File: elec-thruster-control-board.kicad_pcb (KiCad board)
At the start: 2 copper layers, 44 parts, among them J11 Conn_01x02_Socket, J12 Conn_01x02_Socket, J13 Conn_02x05_Counter_Clockwise, J15 Conn_01x02_Socket, J16 Conn_01x02_Socket, J18 Conn_01x02_Socket, J19 Conn_01x02_Socket, J2 Conn_01x02_Socket, J20 Conn_01x02_Socket, J21 Conn_01x02_Socket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

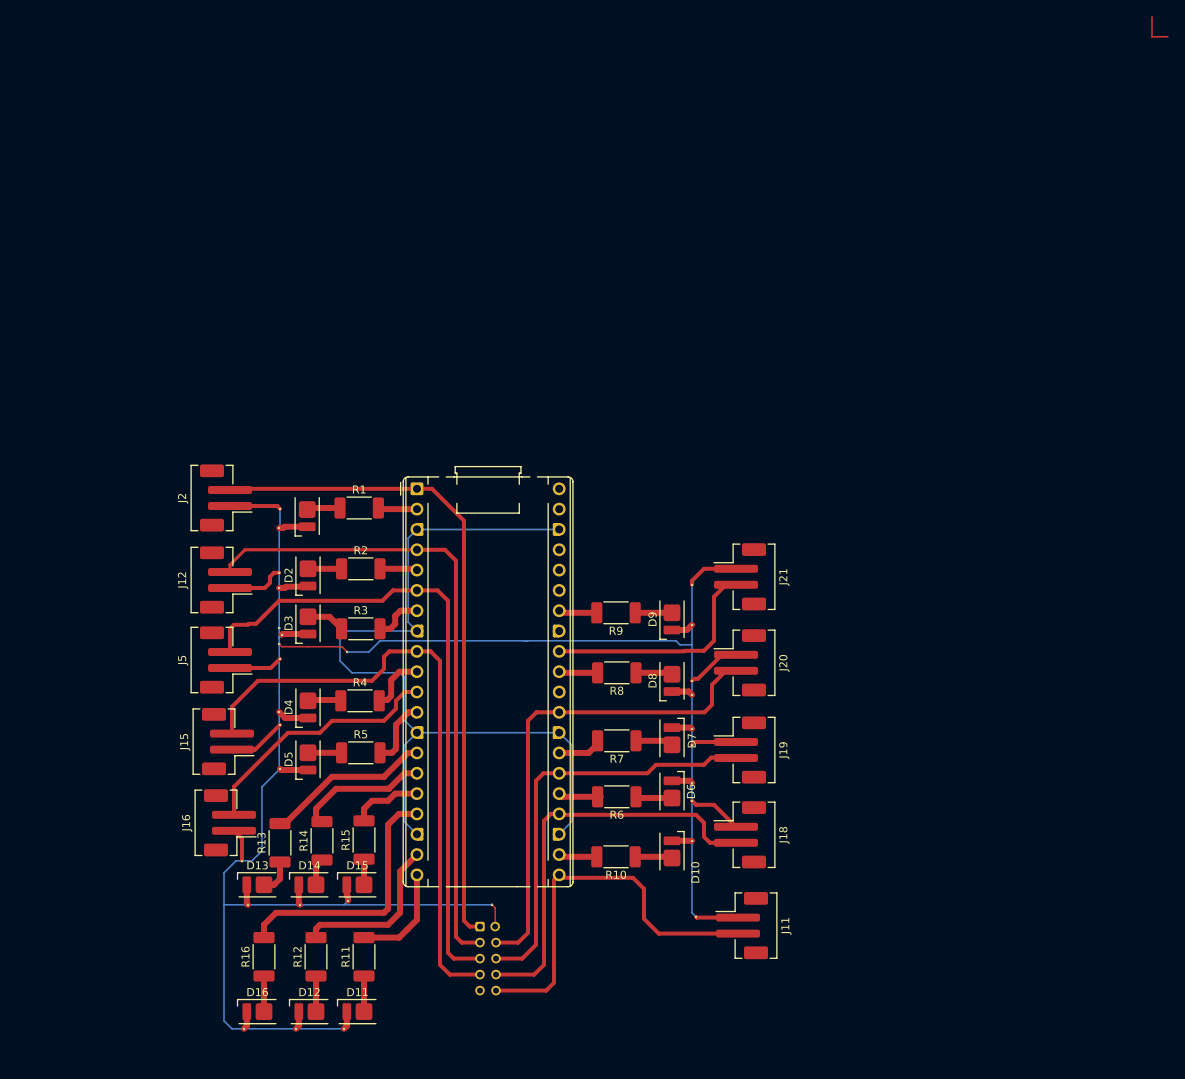
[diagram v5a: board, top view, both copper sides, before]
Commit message: This is based on a modified version of Dilraj's circuit.
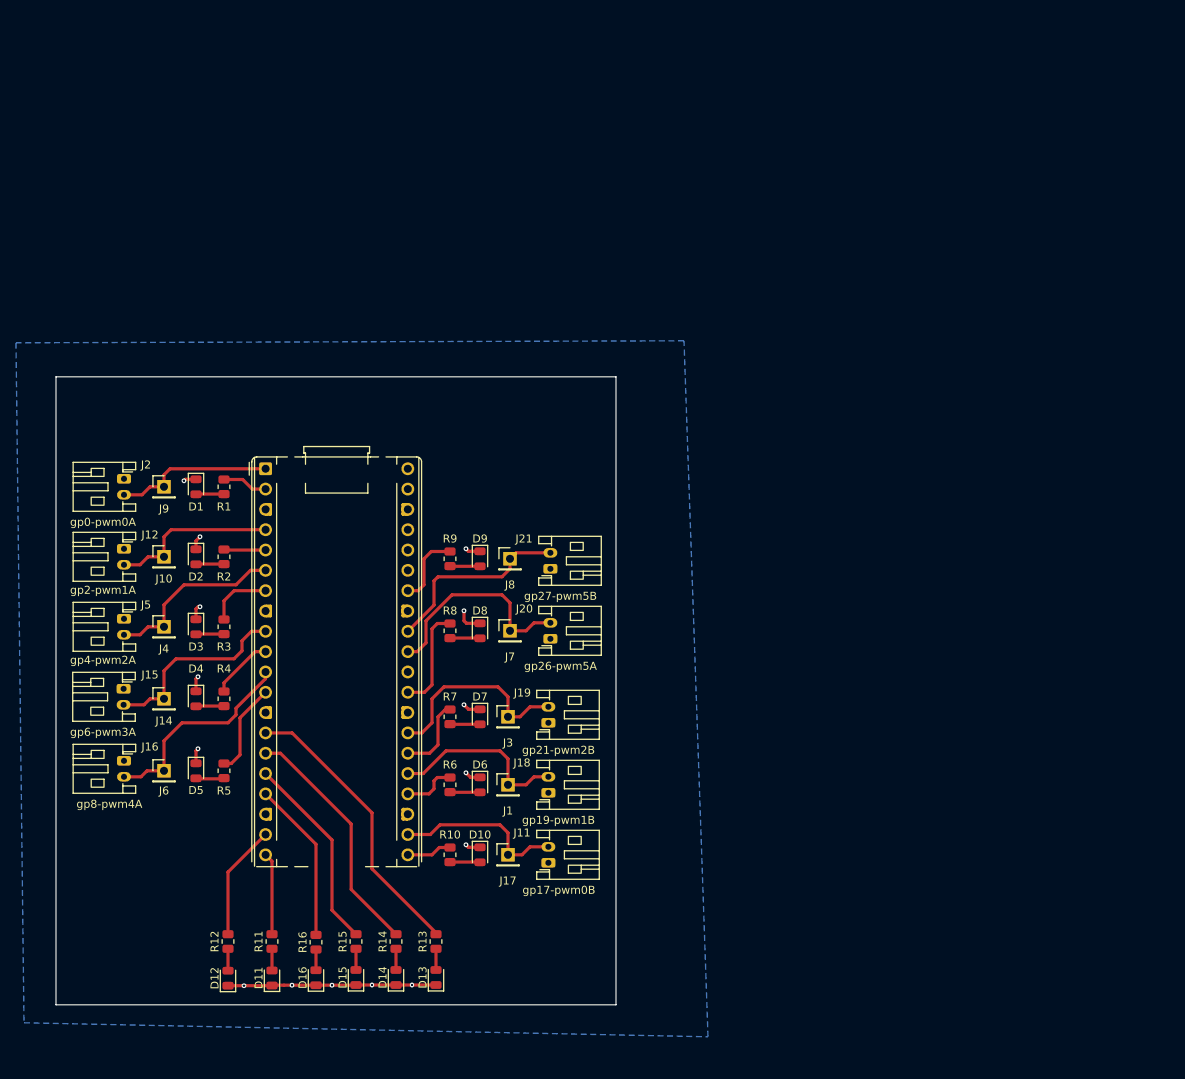
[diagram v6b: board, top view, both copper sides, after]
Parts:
- removed J13: Conn_02x05_Counter_Clockwise, Connector_JST:JST_PHD_B10B-PHDSS_2x05_P2.00mm_Vertical
- added J1: Conn_01x01, Connector_PinHeader_2.54mm:PinHeader_1x01_P2.54mm_Vertical, F.Cu at (161.0, 90.5)
- added J10: Conn_01x01, Connector_PinHeader_2.54mm:PinHeader_1x01_P2.54mm_Vertical, F.Cu at (118.0, 62.0)
- added J14: Conn_01x01, Connector_PinHeader_2.54mm:PinHeader_1x01_P2.54mm_Vertical, F.Cu at (118.0, 79.8)
- added J17: Conn_01x01, Connector_PinHeader_2.54mm:PinHeader_1x01_P2.54mm_Vertical, F.Cu at (161.0, 99.2)
- added J3: Conn_01x01, Connector_PinHeader_2.54mm:PinHeader_1x01_P2.54mm_Vertical, F.Cu at (161.0, 82.0)
- added J4: Conn_01x01, Connector_PinHeader_2.54mm:PinHeader_1x01_P2.54mm_Vertical, F.Cu at (118.0, 70.8)
- added J6: Conn_01x01, Connector_PinHeader_2.54mm:PinHeader_1x01_P2.54mm_Vertical, F.Cu at (118.0, 88.8)
- added J7: Conn_01x01, Connector_PinHeader_2.54mm:PinHeader_1x01_P2.54mm_Vertical, F.Cu at (161.2, 71.2)
- added J8: Conn_01x01, Connector_PinHeader_2.54mm:PinHeader_1x01_P2.54mm_Vertical, F.Cu at (161.2, 62.2)
- added J9: Conn_01x01, Connector_PinHeader_2.54mm:PinHeader_1x01_P2.54mm_Vertical, F.Cu at (118.0, 53.2)
- D1, D10, D11, D12, D13, D14, D15, D16, D2, D3, D4, D5, D6, D7, D8, D9: footprint LED_SMD:LED_Everlight-SMD3528_3.5x2.8mm_67-21ST -> LED_SMD:LED_0805_2012Metric
- J11: value Conn_01x02_Socket -> gp17-pwm0B; footprint Connector_JST:JST_PH_B2B-PH-SM4-TB_1x02-1MP_P2.00mm_Vertical -> Library:LABELED_JST_PH_S2B-PH-K_1x02_P2.00mm_Horizontal
- J12: value Conn_01x02_Socket -> gp2-pwm1A; footprint Connector_JST:JST_PH_B2B-PH-SM4-TB_1x02-1MP_P2.00mm_Vertical -> Library:LABELED_JST_PH_S2B-PH-K_1x02_P2.00mm_Horizontal
- J15: value Conn_01x02_Socket -> gp6-pwm3A; footprint Connector_JST:JST_PH_B2B-PH-SM4-TB_1x02-1MP_P2.00mm_Vertical -> Library:LABELED_JST_PH_S2B-PH-K_1x02_P2.00mm_Horizontal
- J16: value Conn_01x02_Socket -> gp8-pwm4A; footprint Connector_JST:JST_PH_B2B-PH-SM4-TB_1x02-1MP_P2.00mm_Vertical -> Library:LABELED_JST_PH_S2B-PH-K_1x02_P2.00mm_Horizontal
- J18: value Conn_01x02_Socket -> gp19-pwm1B; footprint Connector_JST:JST_PH_B2B-PH-SM4-TB_1x02-1MP_P2.00mm_Vertical -> Library:LABELED_JST_PH_S2B-PH-K_1x02_P2.00mm_Horizontal
- J19: value Conn_01x02_Socket -> gp21-pwm2B; footprint Connector_JST:JST_PH_B2B-PH-SM4-TB_1x02-1MP_P2.00mm_Vertical -> Library:LABELED_JST_PH_S2B-PH-K_1x02_P2.00mm_Horizontal
- J2: value Conn_01x02_Socket -> gp0-pwm0A; footprint Connector_JST:JST_PH_B2B-PH-SM4-TB_1x02-1MP_P2.00mm_Vertical -> Library:LABELED_JST_PH_S2B-PH-K_1x02_P2.00mm_Horizontal
- J20: value Conn_01x02_Socket -> gp26-pwm5A; footprint Connector_JST:JST_PH_B2B-PH-SM4-TB_1x02-1MP_P2.00mm_Vertical -> Library:LABELED_JST_PH_S2B-PH-K_1x02_P2.00mm_Horizontal
- J21: value Conn_01x02_Socket -> gp27-pwm5B; footprint Connector_JST:JST_PH_B2B-PH-SM4-TB_1x02-1MP_P2.00mm_Vertical -> Library:LABELED_JST_PH_S2B-PH-K_1x02_P2.00mm_Horizontal
- J5: value Conn_01x02_Socket -> gp4-pwm2A; footprint Connector_JST:JST_PH_B2B-PH-SM4-TB_1x02-1MP_P2.00mm_Vertical -> Library:LABELED_JST_PH_S2B-PH-K_1x02_P2.00mm_Horizontal
- R1, R10, R11, R12, R13, R14, R15, R16, R2, R3, R4, R5, R6, R7, R8, R9: footprint Resistor_SMD:R_2010_5025Metric_Pad1.40x2.65mm_HandSolder -> Resistor_SMD:R_0805_2012Metric
- moved J11 25.4 mm to (166.1, 100.2), turned to 90 degrees
- moved D9 25.2 mm to (157.5, 62.2), turned to -90 degrees
- moved D13 25.1 mm to (152.0, 114.6), turned to 90 degrees
- moved D8 24.8 mm to (157.5, 71.2), turned to -90 degrees
- moved J18 24.5 mm to (166.1, 91.5), turned to 90 degrees
- moved J19 24.2 mm to (166.1, 82.8), turned to 90 degrees
- moved D7 24.2 mm to (157.5, 82.0)
- moved D6 24.0 mm to (157.5, 90.5)
- moved D10 24.0 mm to (157.5, 99.2)
- moved J20 23.9 mm to (166.3, 72.2), turned to 90 degrees
- moved J21 23.7 mm to (166.3, 63.5), turned to 90 degrees
- moved R13 23.1 mm to (152.0, 110.1)
- moved R9 21.8 mm to (153.8, 62.2), turned to 90 degrees
- moved R8 21.5 mm to (153.8, 71.2), turned to 90 degrees
- moved R7 21.1 mm to (153.8, 82.0), turned to 90 degrees
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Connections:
- net /gpio0 renamed /gp0-pwm0A
- net /gpio2 renamed /gp2-pwm1A
- net /gpio4 renamed /gp4-pwm2A
- net /gpio6 renamed /gp6-pwm3A
- net /gpio8 renamed /gp8-pwm4A
- net /gpio9_pwm9 renamed /gp27-pwm5B
- A1 pad 13: Net-(A1-GND-Pad13) -> GND
- A1 pad 18: Net-(A1-GND-Pad13) -> GND
- A1 pad 21: /gpio16 -> Net-(A1-GPIO16)
- A1 pad 22: Net-(A1-GPIO17) -> /gp17-pwm0B
- A1 pad 23: Net-(A1-GND-Pad13) -> GND
- A1 pad 24: /gpio18 -> Net-(A1-GPIO18)
- A1 pad 25: Net-(A1-GPIO19) -> /gp19-pwm1B
- A1 pad 26: /gpio20 -> Net-(A1-GPIO20)
- A1 pad 27: Net-(A1-GPIO21) -> /gp21-pwm2B
- A1 pad 28: Net-(A1-GND-Pad13) -> GND
- A1 pad 29: /gpio22 -> Net-(A1-GPIO22)
- A1 pad 3: Net-(A1-GND-Pad13) -> GND
- A1 pad 31: Net-(A1-GPIO26_ADC0) -> /gp26-pwm5A
- A1 pad 33: unconnected-(A1-AGND-Pad33) -> GND
- A1 pad 38: Net-(A1-GND-Pad13) -> GND
- A1 pad 8: Net-(A1-GND-Pad13) -> GND
- J11 pad 2: /gpio16 -> /gp17-pwm0B
- J18 pad 2: /gpio18 -> /gp19-pwm1B
- J19 pad 2: /gpio20 -> /gp21-pwm2B
- J20 pad 2: /gpio22 -> /gp26-pwm5A
- R10 pad 2: Net-(A1-GPIO17) -> Net-(A1-GPIO16)
- R6 pad 2: Net-(A1-GPIO19) -> Net-(A1-GPIO18)
- R7 pad 2: Net-(A1-GPIO21) -> Net-(A1-GPIO20)
- R8 pad 2: Net-(A1-GPIO26_ADC0) -> Net-(A1-GPIO22)
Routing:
- net GND: track 329.2 -> 46.5 mm, vias 30 -> 15
- net Net-(A1-GND-Pad13): track 106.7 -> 0.00 mm
- net /gp0-pwm0A: track 83.7 -> 19.9 mm
- net /gpio22: track 61.6 -> 0.00 mm
- net /gp2-pwm1A: track 80.8 -> 21.0 mm
- net /gp4-pwm2A: track 81.0 -> 22.6 mm
- net /gpio18: track 53.4 -> 0.00 mm
- net /gpio20: track 52.9 -> 0.00 mm
- net /gp6-pwm3A: track 77.1 -> 24.8 mm
- net /gpio16: track 52.2 -> 0.00 mm
- net /gp26-pwm5A: track 0.00 -> 26.7 mm
- net /gp21-pwm2B: track 0.00 -> 25.3 mm
- net /gp19-pwm1B: track 0.00 -> 22.8 mm
- net /gp17-pwm0B: track 0.00 -> 21.7 mm
- net Net-(A1-GPIO12): track 8.91 -> 24.8 mm
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- added copper zone on B.Cu, net GND
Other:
- board outline added: 70 x 78.5 mm

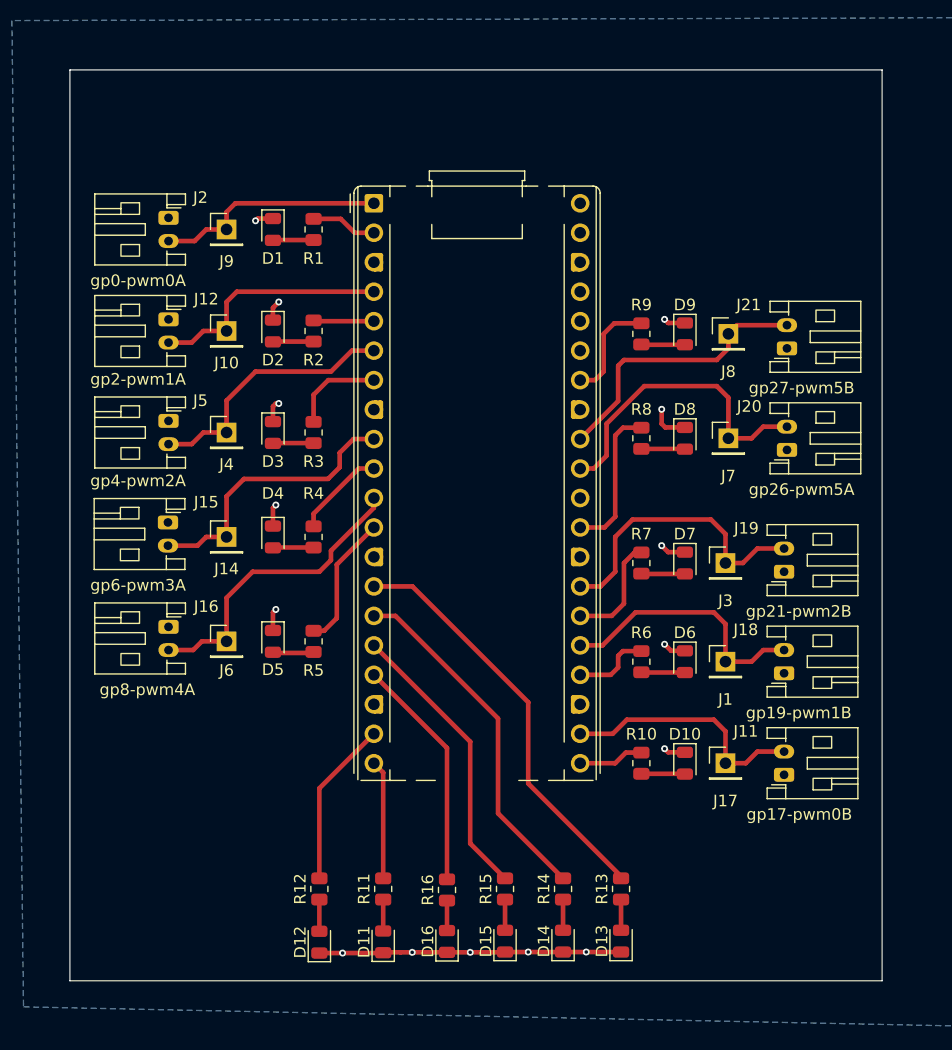
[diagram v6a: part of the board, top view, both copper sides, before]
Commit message: Painstakingly added better silkscreening and MOUNTING HOLES!
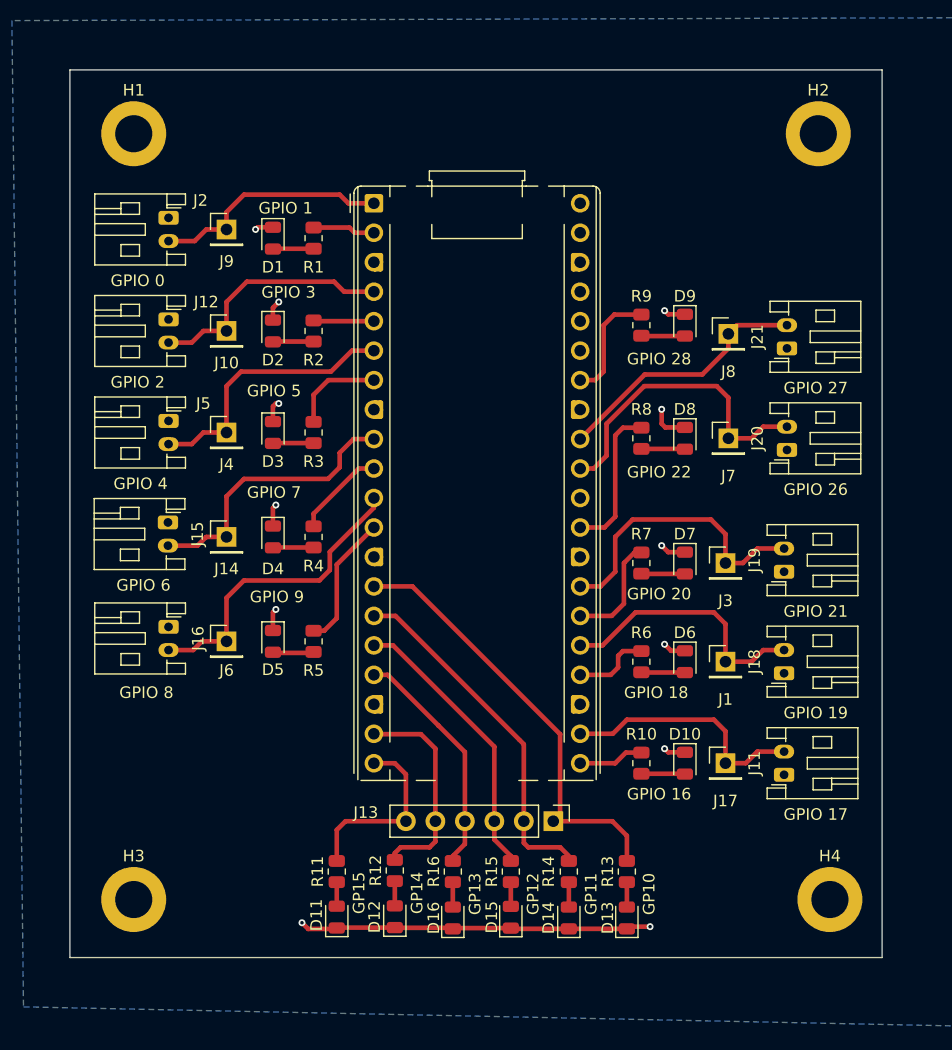
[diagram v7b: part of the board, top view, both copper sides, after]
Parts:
- added H1: MountingHole, MountingHole:MountingHole_3.2mm_M3_DIN965_Pad, F.Cu at (110.0, 45.0)
- added H2: MountingHole, MountingHole:MountingHole_3.2mm_M3_DIN965_Pad, F.Cu at (169.0, 45.0)
- added H3: MountingHole, MountingHole:MountingHole_3.2mm_M3_DIN965_Pad, F.Cu at (110.0, 111.0)
- added H4: MountingHole, MountingHole:MountingHole_3.2mm_M3_DIN965_Pad, F.Cu at (170.0, 111.0)
- added J13: Conn_01x06, Connector_PinHeader_2.54mm:PinHeader_1x06_P2.54mm_Vertical, F.Cu at (146.2, 104.2)
- J11, J12, J15, J16, J18, J19, J2, J20, J21, J5: footprint Library:LABELED_JST_PH_S2B-PH-K_1x02_P2.00mm_Horizontal -> Connector_JST:JST_PH_S2B-PH-K_1x02_P2.00mm_Horizontal
- moved D12 6.86 mm to (132.5, 112.5)
- moved R12 6.69 mm to (132.5, 108.5)
- moved D11 4.54 mm to (127.5, 112.5)
- moved R11 4.27 mm to (127.5, 108.6)
- moved D15 2.12 mm to (142.5, 112.5)
- moved D16 2.09 mm to (137.5, 112.6)
- moved D13 2.06 mm to (152.5, 112.6)
- moved D14 2.06 mm to (147.5, 112.6)
- moved R16 1.66 mm to (137.5, 108.6)
- moved R13 1.58 mm to (152.5, 108.6)
- moved R14 1.58 mm to (147.5, 108.6)
- moved R15 1.58 mm to (142.5, 108.6)
- moved D1 0.75 mm to (122.0, 54.0)
- moved D9 0.75 mm to (157.5, 61.5)
- moved R1 0.75 mm to (125.5, 54.0)
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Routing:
- net Net-(A1-GPIO15): track 10.3 -> 16.1 mm
- net GND: track 46.5 -> 50.9 mm, vias 15 -> 12
- net Net-(A1-GPIO14): track 14.4 -> 18.3 mm
- net Net-(A1-GPIO10): track 35.9 -> 38.1 mm
- net /gp27-pwm5B: track 24.4 -> 22.6 mm
- net Net-(A1-GPIO28_ADC2): track 9.20 -> 9.95 mm
- net /gp4-pwm2A: track 22.6 -> 23.4 mm
- net /gp2-pwm1A: track 21.0 -> 21.7 mm
- net /gp0-pwm0A: track 19.9 -> 20.5 mm
- net Net-(D12-A): track 2.74 -> 2.13 mm
- net Net-(D11-A): track 2.71 -> 2.15 mm
- net Net-(D15-A): track 2.65 -> 2.09 mm
- net Net-(D14-A): track 2.65 -> 2.15 mm
- net Net-(D13-A): track 2.65 -> 2.15 mm
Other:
- board size 70 x 78.5 mm -> 70 x 76.5 mm
- board text added: "GP10"
- board text added: "GP11"
- board text added: "GP12"
- board text added: "GP13"
- board text added: "GP14"
- board text added: "GP15"
- board text added: "GPIO 0"
- board text added: "GPIO 1"
- board text added: "GPIO 16"
- board text added: "GPIO 17"
- board text added: "GPIO 18"
- board text added: "GPIO 19"
- board text added: "GPIO 2"
- board text added: "GPIO 20"
- board text added: "GPIO 21"
- board text added: "GPIO 22"
- board text added: "GPIO 26"
- board text added: "GPIO 27"
- board text added: "GPIO 28"
- board text added: "GPIO 3"
- board text added: "GPIO 4"
- board text added: "GPIO 5"
- board text added: "GPIO 6"
- board text added: "GPIO 7"
- board text added: "GPIO 8"
- board text added: "GPIO 9"

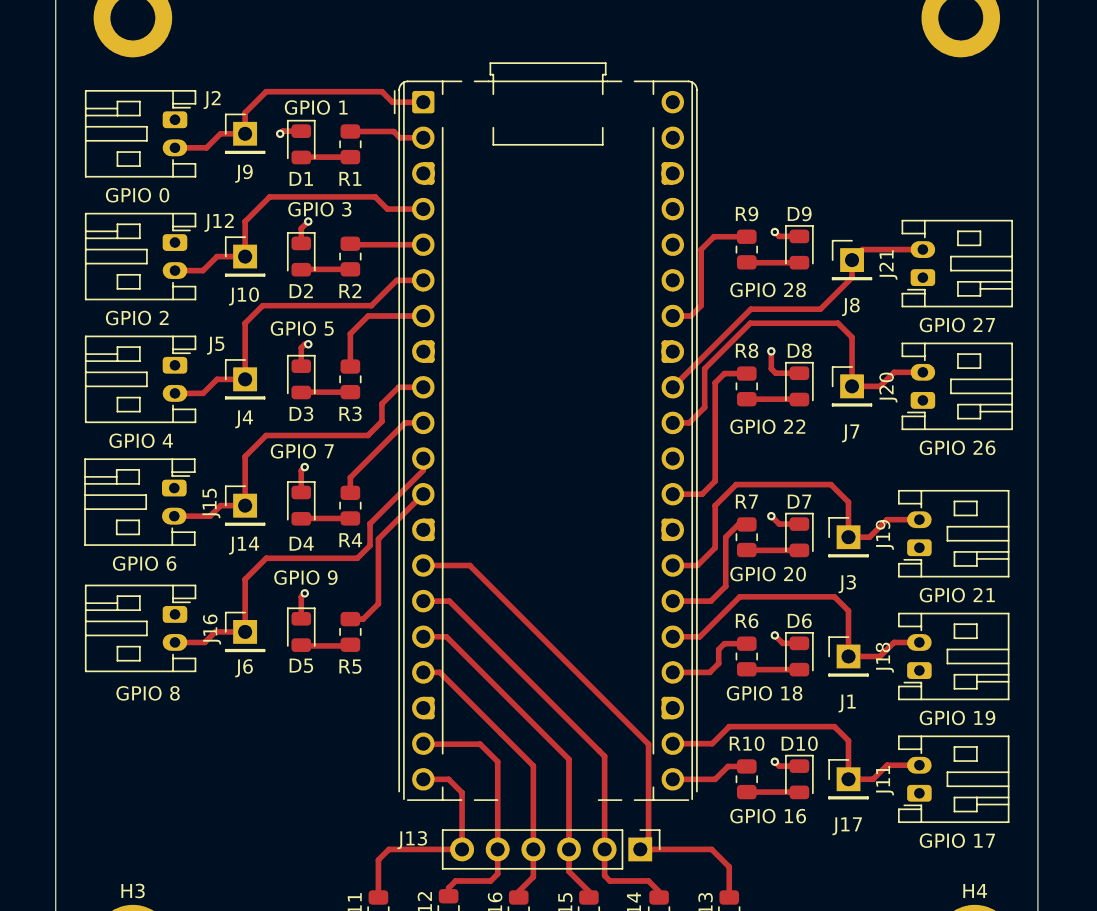
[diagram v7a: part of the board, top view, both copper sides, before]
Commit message: Forgot to push PCB update. Now addded updated PCB with vertical JST connectors
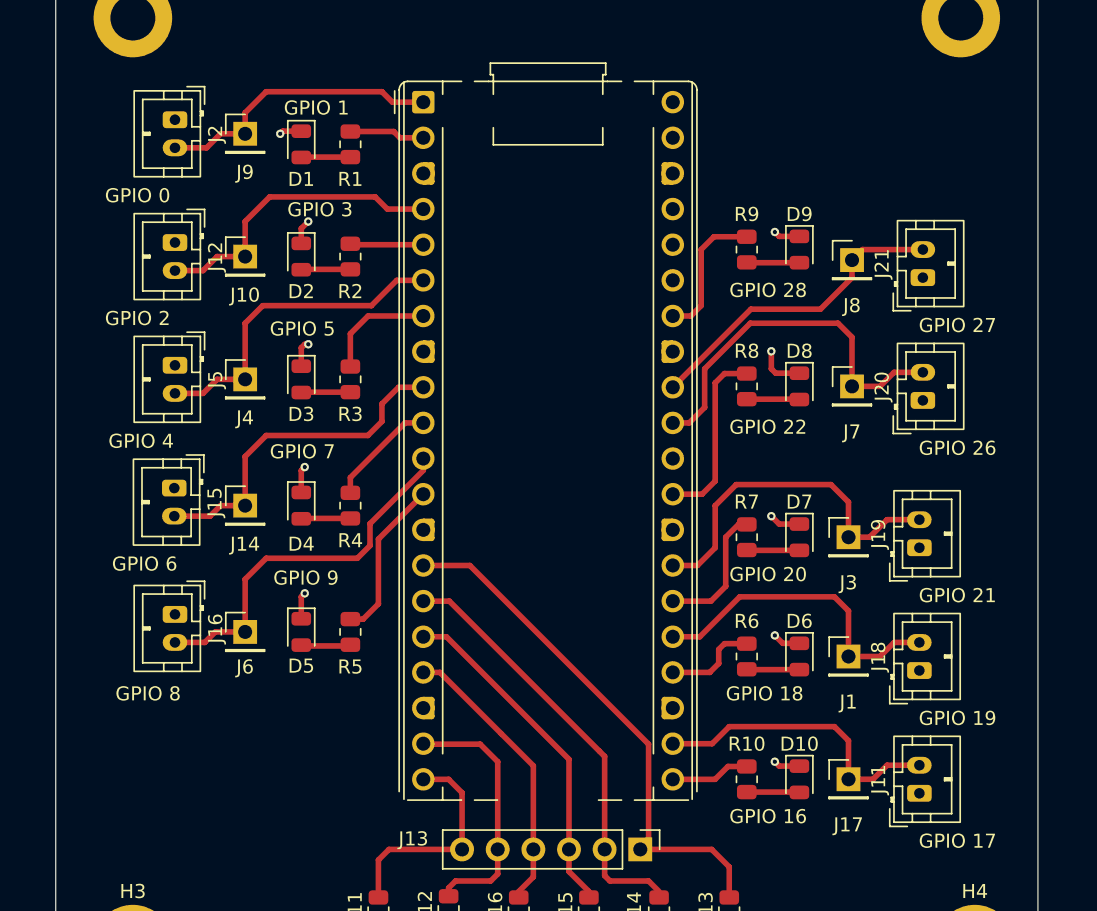
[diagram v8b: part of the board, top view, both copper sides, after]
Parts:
- J11, J12, J15, J16, J18, J19, J2, J20, J21, J5: footprint Connector_JST:JST_PH_S2B-PH-K_1x02_P2.00mm_Horizontal -> Connector_JST:JST_PH_B2B-PH-K_1x02_P2.00mm_Vertical
